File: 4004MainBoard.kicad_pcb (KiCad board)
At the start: 2 copper layers, 95.1 x 72.1 mm, 156 parts, among them J1 BUS, J2 P0 RAM1, J3 CMRAM RAM2, J4 P0 RAM2, J5 DC 5V, Q1 2SA1162GR, Q10 2SC2712GR, Q11 2SA1162GR, Q2 2SC2712GR, Q3 2SA1162GR, Q4 2SC2712GR, Q5 2SA1162GR, Q6 2SA1162GR, Q7 2SA1162GR, Q8 2SA1162GR, Q9 2SC2712GR, SW1 TEST, SW2 RESET, SW3 POWER, U1 74HC08, U2 74HC161, U3 PST600, U4 Intel4004, U5 LT1931A, U6 74LS540, U7 Intel4002-1, U8 Intel4002-1, U9 LT1763, Y1 DLO555MB

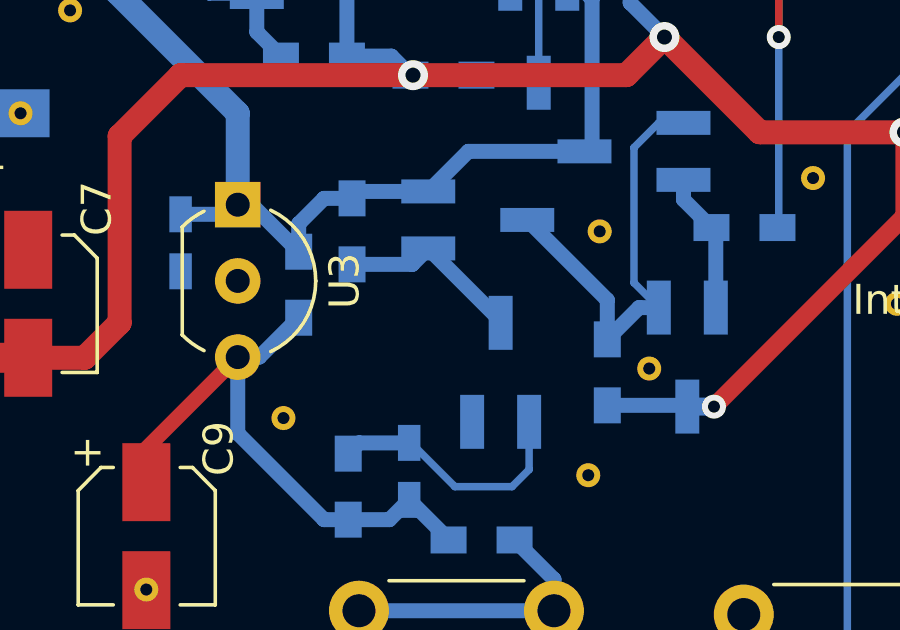
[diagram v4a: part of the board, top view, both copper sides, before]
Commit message: 電源電圧調整 基板修正
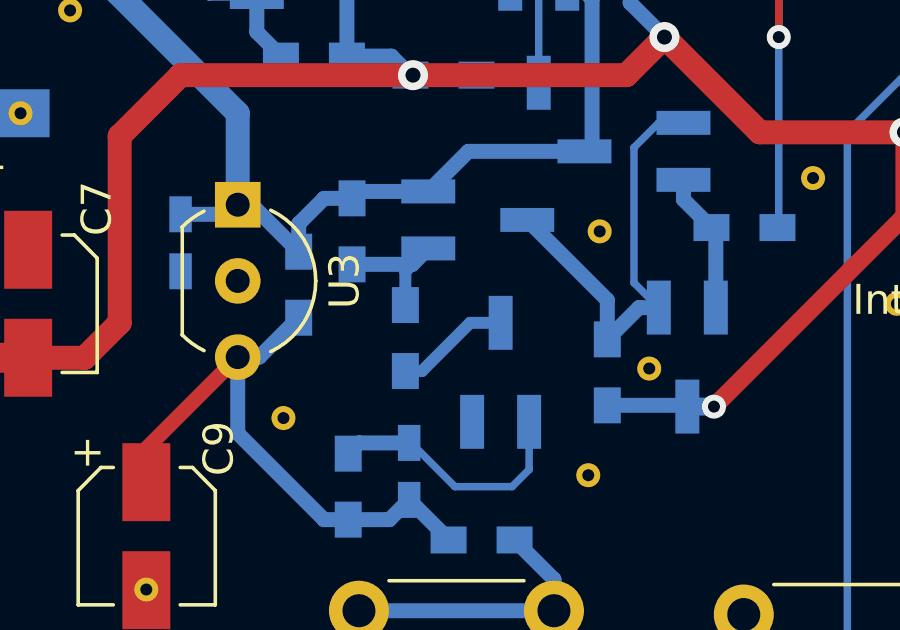
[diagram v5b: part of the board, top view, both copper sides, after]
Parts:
- added R35: 1k, Resistors_SMD:R_0603_HandSoldering, B.Cu at (161.9, 125.1)
- C5: value 100p -> 0
- R14: value 1k -> 0
- R16, R7, R8: value 300 -> 1k
- R25: value 33k -> 30k(33k//330k)
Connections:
- Q8 pad 1: Net-(Q10-Pad3) -> Net-(Q8-Pad1)
- R11 pad 2: Net-(Q10-Pad3) -> Net-(Q8-Pad1)
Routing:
- net Net-(Q8-Pad1): track 0.00 -> 4.21 mm
- net Net-(Q10-Pad3): track 6.24 -> 3.91 mm
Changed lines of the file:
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@@
 (kicad_pcb (version 4) (host pcbnew 4.0.7)
   (general
-    (links 331)
+    (links 332)
     (no_connects 0)
-    (area 114.453999 59.563 238.887001 149.225001)
+    (area 131.369999 71.044999 226.643001 143.331001)
     (thickness 1.6)
     (drawings 76)
-    (tracks 949)
+    (tracks 953)
     (zones 0)
-    (modules 156)
-    (nets 81)
+    (modules 157)
+    (nets 82)
   )
   (page A4)
@@
   (net 79 "Net-(C25-Pad1)")
   (net 80 "Net-(C25-Pad2)")
+  (net 81 "Net-(Q8-Pad1)")
   (net_class Default "This is the default net class."
     (clearance 0.2)
@@
     (add_net "Net-(Q4-Pad2)")
     (add_net "Net-(Q7-Pad3)")
+    (add_net "Net-(Q8-Pad1)")
     (add_net "Net-(R15-Pad1)")
     (add_net "Net-(U1-Pad12)")
@@
       (effects (font (size 1 1) (thickness 0.15)) (justify mirror))
     )
-    (fp_text value 100p (at 0 -1.5 270) (layer B.Fab)
+    (fp_text value 0 (at 0 -1.5 270) (layer B.Fab)
       (effects (font (size 1 1) (thickness 0.15)) (justify mirror))
     )
@@
     (fp_line (start 2.8 -1.8) (end -2.8 -1.8) (layer B.CrtYd) (width 0.05))
     (pad 1 smd rect (at -1.65 0.95) (size 1.8 0.8) (layers B.Cu B.Paste B.Mask)
-      (net 61 "Net-(Q10-Pad3)"))
+      (net 81 "Net-(Q8-Pad1)"))
     (pad 2 smd rect (at -1.65 -0.95) (size 1.8 0.8) (layers B.Cu B.Paste B.Mask)
       (net 1 VCC))
@@
     (tags "SC-59 hand-soldering")
     (attr smd)
-    (fp_text reference Q10 (at 0.254 -2.286 90) (layer B.SilkS)
+    (fp_text reference Q10 (at -3.556 0.762 180) (layer B.SilkS)
       (effects (font (size 1 1) (thickness 0.15)) (justify mirror))
     )
@@
       (effects (font (size 1 1) (thickness 0.15)) (justify mirror))
     )
-    (fp_text value 300 (at 0 -1.55) (layer B.Fab)
+    (fp_text value 1k (at 0 -1.55) (layer B.Fab)
       (effects (font (size 1 1) (thickness 0.15)) (justify mirror))
     )
@@
       (effects (font (size 1 1) (thickness 0.15)) (justify mirror))
     )
-    (fp_text value 300 (at 0 -1.55 180) (layer B.Fab)
+    (fp_text value 1k (at 0 -1.55 180) (layer B.Fab)
       (effects (font (size 1 1) (thickness 0.15)) (justify mirror))
     )
@@
     (tags "resistor 0603")
     (attr smd)
-    (fp_text reference R11 (at 3.429 -0.381 270) (layer B.SilkS)
+    (fp_text reference R11 (at -3.175 -0.381 270) (layer B.SilkS)
       (effects (font (size 1 1) (thickness 0.15)) (justify mirror))
     )
@@
       (net 1 VCC))
     (pad 2 smd rect (at 1.1 0 270) (size 1.2 0.9) (layers B.Cu B.Paste B.Mask)
-      (net 61 "Net-(Q10-Pad3)"))
+      (net 81 "Net-(Q8-Pad1)"))
     (model ${KISYS3DMOD}/Resistors_SMD.3dshapes/R_0603.wrl
       (at (xyz 0 0 0))
@@
     (tags "resistor 0603")
     (attr smd)
-    (fp_text reference R12 (at -3.429 0.381 90) (layer B.SilkS)
+    (fp_text reference R12 (at 3.81 0.127 90) (layer B.SilkS)
       (effects (font (size 1 1) (thickness 0.15)) (justify mirror))
     )
@@
       (effects (font (size 1 1) (thickness 0.15)) (justify mirror))
     )
-    (fp_text value 1k (at 0 -1.55 270) (layer B.Fab)
+    (fp_text value 0 (at 0 -1.55 270) (layer B.Fab)
       (effects (font (size 1 1) (thickness 0.15)) (justify mirror))
     )
@@
       (effects (font (size 1 1) (thickness 0.15)) (justify mirror))
     )
-    (fp_text value 300 (at 0 -1.55 270) (layer B.Fab)
+    (fp_text value 1k (at 0 -1.55 270) (layer B.Fab)
       (effects (font (size 1 1) (thickness 0.15)) (justify mirror))
     )
@@
       (effects (font (size 1 1) (thickness 0.15)) (justify mirror))
     )
-    (fp_text value 33k (at 0 -1.55 180) (layer B.Fab)
+    (fp_text value "30k(33k//330k)" (at 0 -1.55 180) (layer B.Fab)
       (effects (font (size 1 1) (thickness 0.15)) (justify mirror))
     )
@@
     )
   )
+  (module Resistors_SMD:R_0603_HandSoldering (layer B.Cu)
+    (at 161.925 125.095 90)
+    (descr "Resistor SMD 0603, hand soldering")
+    (tags "resistor 0603")
+    (attr smd)
+    (fp_text reference R35 (at -1.143 -1.27 90) (layer B.SilkS)
+      (effects (font (size 1 1) (thickness 0.15)) (justify mirror))
+    )
+    (fp_text value 1k (at 0 -1.55 90) (layer B.Fab)
+      (effects (font (size 1 1) (thickness 0.15)) (justify mirror))
+    )
+    (fp_text user %R (at 0 0 90) (layer B.Fab)
+      (effects (font (size 0.4 0.4) (thickness 0.075)) (justify mirror))
+    )
+    (fp_line (start -0.8 -0.4) (end -0.8 0.4) (layer B.Fab) (width 0.1))
+    (fp_line (start 0.8 -0.4) (end -0.8 -0.4) (layer B.Fab) (width 0.1))
+    (fp_line (start 0.8 0.4) (end 0.8 -0.4) (layer B.Fab) (width 0.1))
+    (fp_line (start -0.8 0.4) (end 0.8 0.4) (layer B.Fab) (width 0.1))
+    (fp_line (start 0.5 -0.68) (end -0.5 -0.68) (layer B.SilkS) (width 0.12))
+    (fp_line (start -0.5 0.68) (end 0.5 0.68) (layer B.SilkS) (width 0.12))
+    (fp_line (start -1.96 0.7) (end 1.95 0.7) (layer B.CrtYd) (width 0.05))
+    (fp_line (start -1.96 0.7) (end -1.96 -0.7) (layer B.CrtYd) (width 0.05))
+    (fp_line (start 1.95 -0.7) (end 1.95 0.7) (layer B.CrtYd) (width 0.05))
+    (fp_line (start 1.95 -0.7) (end -1.96 -0.7) (layer B.CrtYd) (width 0.05))
+    (pad 1 smd rect (at -1.1 0 90) (size 1.2 0.9) (layers B.Cu B.Paste B.Mask)
+      (net 61 "Net-(Q10-Pad3)"))
+    (pad 2 smd rect (at 1.1 0 90) (size 1.2 0.9) (layers B.Cu B.Paste B.Mask)
+      (net 81 "Net-(Q8-Pad1)"))
+    (model ${KISYS3DMOD}/Resistors_SMD.3dshapes/R_0603.wrl
+      (at (xyz 0 0 0))
+      (scale (xyz 1 1 1))
+      (rotate (xyz 0 0 0))
+    )
+  )
   (gr_line (start 144.272 90.551) (end 144.272 88.011) (angle 90) (layer B.Mask) (width 1))
   (gr_line (start 142.113 90.551) (end 144.272 90.551) (angle 90) (layer B.Mask) (width 1))
@@
   (segment (start 161.29 98.552) (end 161.29 89.281) (width 0.25) (layer F.Cu) (net 60))
   (segment (start 160.401 99.441) (end 161.29 98.552) (width 0.25) (layer F.Cu) (net 60))
+  (segment (start 161.925 126.195) (end 162.476 126.195) (width 0.4) (layer B.Cu) (net 61))
+  (segment (start 164.083 124.588) (end 165.1 124.588) (width 0.4) (layer B.Cu) (net 61))
+  (segment (start 162.476 126.195) (end 164.083 124.588) (width 0.4) (layer B.Cu) (net 61))
   (segment (start 165.1 124.588) (end 165.1 124.52) (width 0.5) (layer B.Cu) (net 61) (status 30))
-  (segment (start 165.1 124.52) (end 162.688 122.108) (width 0.5) (layer B.Cu) (net 61) (status 30))
-  (segment (start 160.147 122.639) (end 162.157 122.639) (width 0.5) (layer B.Cu) (net 61) (status 10))
-  (segment (start 162.157 122.639) (end 162.688 122.108) (width 0.5) (layer B.Cu) (net 61) (status 20))
   (segment (start 170.373 124.08) (end 169.714 124.08) (width 0.5) (layer B.Cu) (net 62) (status 10))
   (segment (start 169.714 124.08) (end 168.656 125.138) (width 0.5) (layer B.Cu) (net 62) (status 20))
@@
   (segment (start 162.433 101.473) (end 162.433 89.662) (width 0.25) (layer F.Cu) (net 80))
   (segment (start 160.655 103.251) (end 162.433 101.473) (width 0.25) (layer F.Cu) (net 80))
+  (segment (start 161.925 123.995) (end 161.925 122.871) (width 0.4) (layer B.Cu) (net 81))
+  (segment (start 161.925 122.871) (end 162.157 122.639) (width 0.4) (layer B.Cu) (net 81))
+  (segment (start 160.147 122.639) (end 162.157 122.639) (width 0.5) (layer B.Cu) (net 81) (status 10))
+  (segment (start 162.157 122.639) (end 162.688 122.108) (width 0.5) (layer B.Cu) (net 81) (status 20))
   (zone (net 2) (net_name GND) (layer F.Cu) (hatch edge 0.508)
     (connect_pads (clearance 0.38))
